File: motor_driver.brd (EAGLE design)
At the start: 45.1 x 30.2 mm, 43 parts, among them IC1 LM2936DT-5.0, X1 22-23-2021

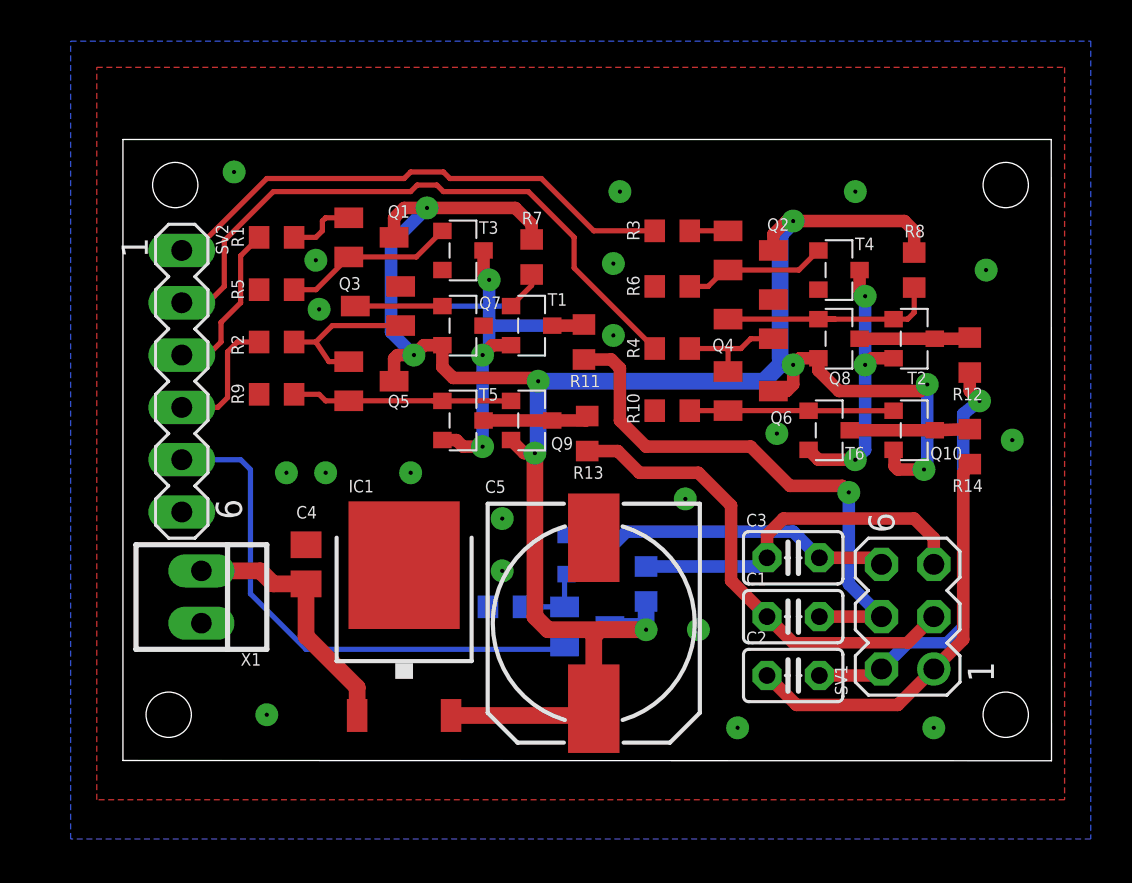
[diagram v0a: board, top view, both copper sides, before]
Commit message: changed resistors in m1, m2 drivers
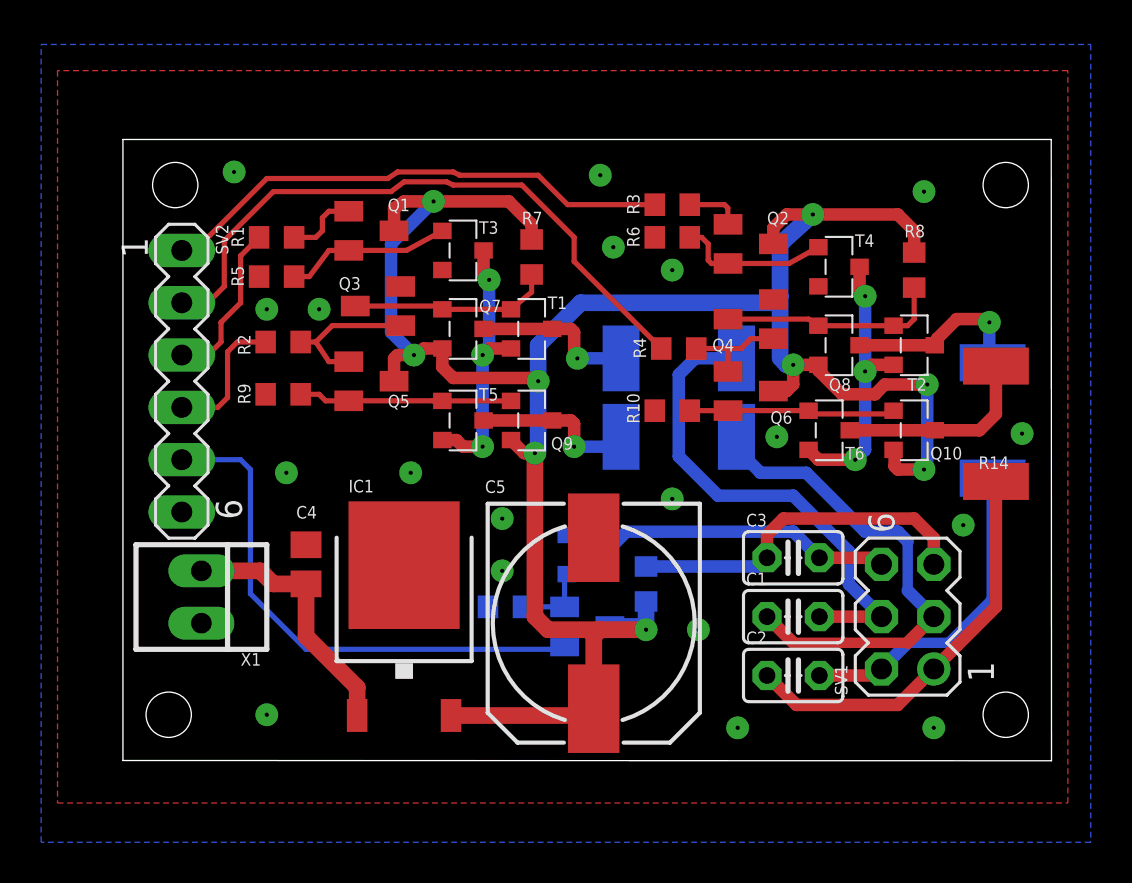
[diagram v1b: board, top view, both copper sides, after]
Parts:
- R11, R12, R13, R14: device rcl:R0603 -> rcl:R2512
- moved R11 4.67 mm to (27.0, 19.5), flipped to the bottom, turned to 0 degrees
- moved R13 4.45 mm to (27.0, 15.7), flipped to the bottom, turned to 0 degrees
- moved R12 3.36 mm to (42.2, 16.5), flipped to the bottom
- moved R6 2.38 mm to (26.7, 25.4)
- moved R14 1.69 mm to (42.4, 16.4)
- moved R3 1.27 mm to (26.7, 27.0)
- moved R5 0.64 mm to (7.46, 23.5)
- moved Q1 0.32 mm to (12.1, 25.7)
- moved Q8 0.32 mm to (34.8, 20.2)
- moved T2 0.32 mm to (38.4, 20.2)
- moved R2 0.32 mm to (7.78, 20.3)
- moved R9 0.32 mm to (7.78, 17.8)
- moved Q2 0.32 mm to (30.5, 25.1)
- moved R4 0.32 mm to (27.0, 20.0)
- moved Q7 0.16 mm to (16.5, 21.0)
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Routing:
- net MN1: track 20.9 -> 15.9 mm, vias 1 -> 0
- net N$2: track 5.83 -> 9.75 mm
- net N$3: track 5.37 -> 9.02 mm, vias 0 -> 1
- net VDD: track 105.4 -> 108.5 mm
- net N$9: track 5.01 -> 7.92 mm, vias 0 -> 1
- net N$8: track 5.20 -> 8.01 mm, vias 0 -> 1
- net MN2: track 26.7 -> 24.1 mm, vias 1 -> 0
- net N$33: track 12.0 -> 10.8 mm
- net N$11: track 1.86 -> 2.72 mm
- net MP2: track 23.3 -> 24.1 mm
- net M1_EN: track 25.7 -> 25.1 mm

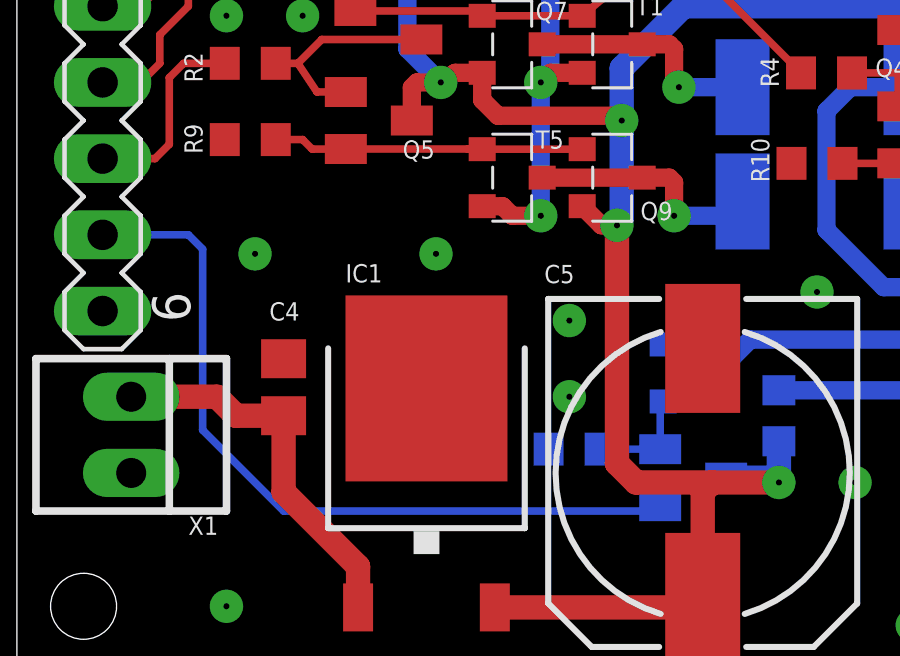
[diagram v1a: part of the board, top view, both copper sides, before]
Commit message: added LED, added bom
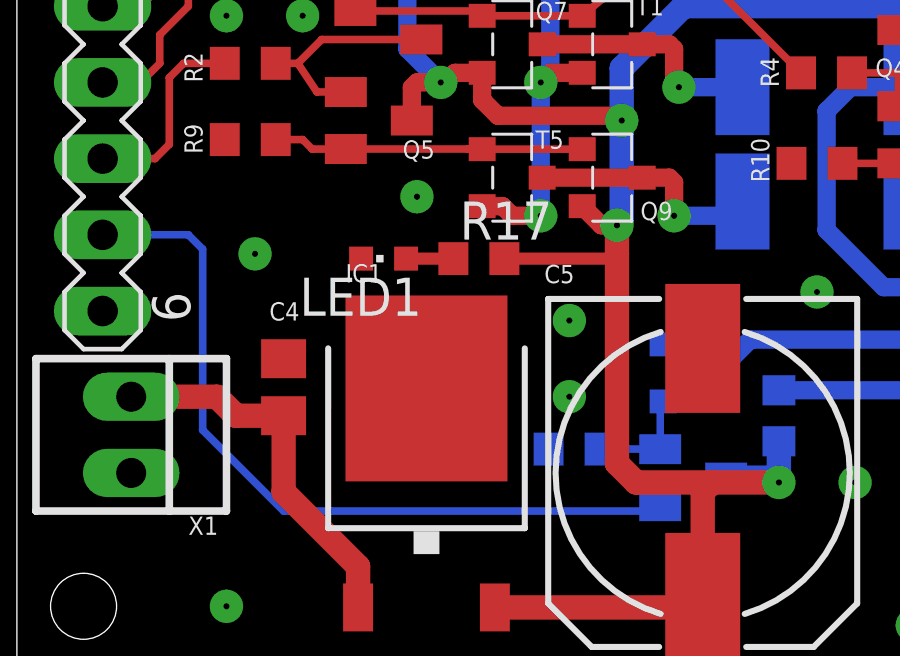
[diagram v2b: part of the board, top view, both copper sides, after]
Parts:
- added LED1: (no value), led:CHIPLED_0603
- added R17: 1k, rcl:R0603
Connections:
- new net N$17: LED1.A, R17.1
- net GND: now also LED1.C
- net VDD: now also R17.2
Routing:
- net VDD: track 108.5 -> 112.4 mm
- net N$17: track 0.00 -> 1.57 mm
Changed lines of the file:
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@@
 <attribute name="VALUE" x="-1.27" y="10.4775" size="1.016" layer="27" ratio="10" rot="R270"/>
 </element>
+<element name="LED1" library="led" package="CHIPLED_0603" value="" x="12.22375" y="13.81125" rot="R90"/>
+<element name="R17" library="rcl" package="R0603" value="1k" x="15.39875" y="13.81125"/>
 </elements>
 <signals>
@@
 <via x="18.415" y="11.7475" extent="1-16" drill="0.2"/>
 <via x="27.94" y="6.35" extent="1-16" drill="0.2"/>
-<via x="13.97" y="13.97" extent="1-16" drill="0.2"/>
+<via x="13.335" y="15.875" extent="1-16" drill="0.2"/>
 <via x="6.985" y="21.9075" extent="1-16" drill="0.2"/>
 <via x="7.9375" y="13.97" extent="1-16" drill="0.2"/>
@@
 <via x="5.3975" y="28.575" extent="1-16" drill="0.2"/>
 <via x="9.525" y="21.9075" extent="1-16" drill="0.2"/>
+<contactref element="LED1" pad="C"/>
 </signal>
 <signal name="MP1">
@@
 <wire x1="23.6425" y1="6.50875" x2="25.24125" y2="6.50875" width="0.8128" layer="16"/>
 <wire x1="25.24125" y1="6.50875" x2="25.4" y2="6.35" width="0.8128" layer="16"/>
-<wire x1="20.0025" y1="14.9225" x2="20.0025" y2="6.985" width="0.8128" layer="1"/>
+<wire x1="20.0025" y1="14.9225" x2="20.0025" y2="13.97" width="0.8128" layer="1"/>
+<wire x1="20.0025" y1="13.97" x2="20.0025" y2="6.985" width="0.8128" layer="1"/>
 <wire x1="20.0025" y1="6.985" x2="20.6375" y2="6.35" width="0.8128" layer="1"/>
 <wire x1="20.6375" y1="6.35" x2="23.1775" y2="6.35" width="0.8128" layer="1"/>
@@
 <wire x1="36.5125" y1="17.78" x2="36.98875" y2="18.25625" width="0.6096" layer="1"/>
 <wire x1="36.98875" y1="18.25625" x2="39.0525" y2="18.25625" width="0.6096" layer="1"/>
+<contactref element="R17" pad="2"/>
+<wire x1="16.24875" y1="13.81125" x2="20.0025" y2="13.81125" width="0.4064" layer="1"/>
+<wire x1="20.0025" y1="13.81125" x2="20.0025" y2="13.97" width="0.4064" layer="1"/>
 </signal>
 <signal name="N$6">
@@
 <wire x1="11.3725" y1="3.55" x2="8.89" y2="6.0325" width="0.8128" layer="1"/>
 </signal>
+<signal name="N$17">
+<contactref element="R17" pad="1"/>
+<contactref element="LED1" pad="A"/>
+<wire x1="12.97375" y1="13.81125" x2="14.54875" y2="13.81125" width="0.4064" layer="1"/>
+</signal>
 </signals>
